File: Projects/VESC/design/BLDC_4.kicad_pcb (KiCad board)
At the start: 4 copper layers, 116 parts, among them P10 AMP17614426-2_EDGE, Q1 IRFS7530, Q2 IRFS7530, Q3 IRFS7530, Q4 IRFS7530, Q5 IRFS7530, Q6 IRFS7530, U1 STM32F40X_LQFP64, U2 TC2117, U3 DRV8302, U401 MCP2562FD, X2 CRYSTAL_GROUND_PIN

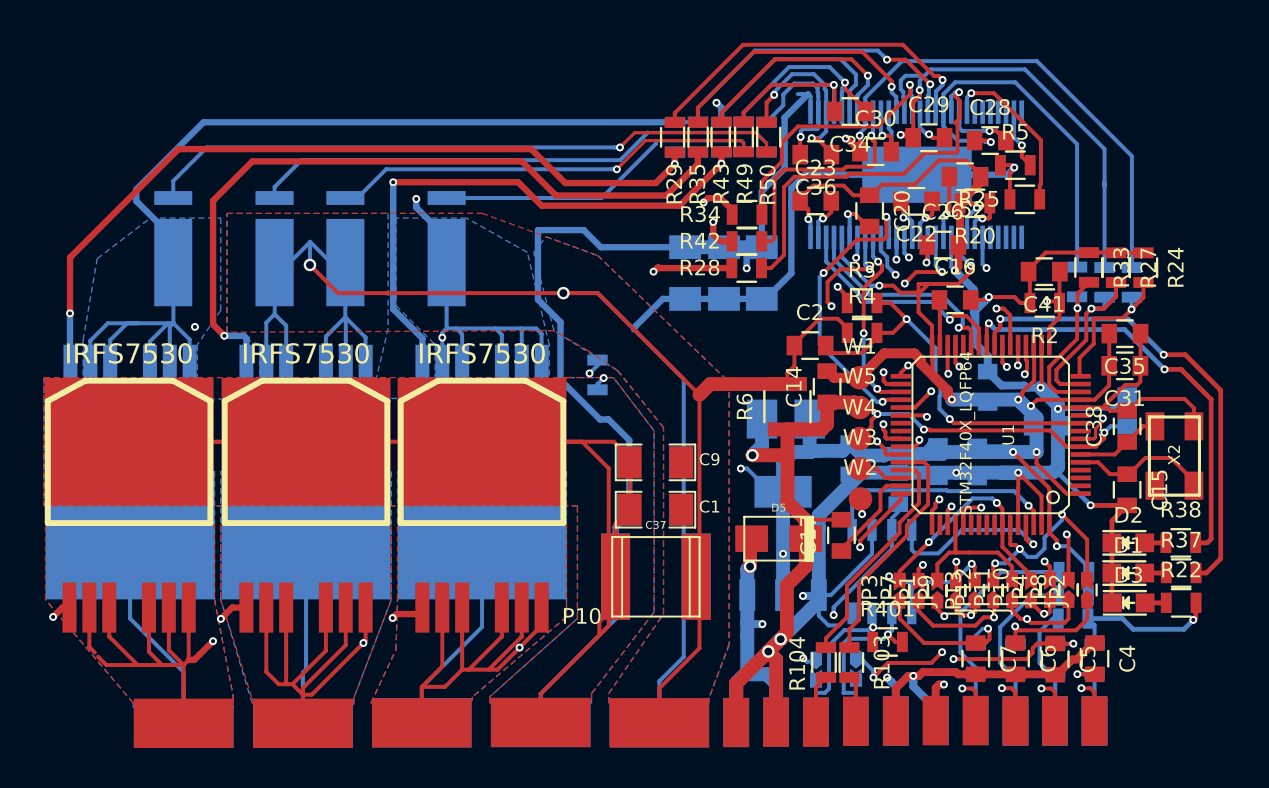
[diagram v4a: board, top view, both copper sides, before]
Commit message: more VESC card cleanup - still need to fix ground planes, via stiching, and silkscreen
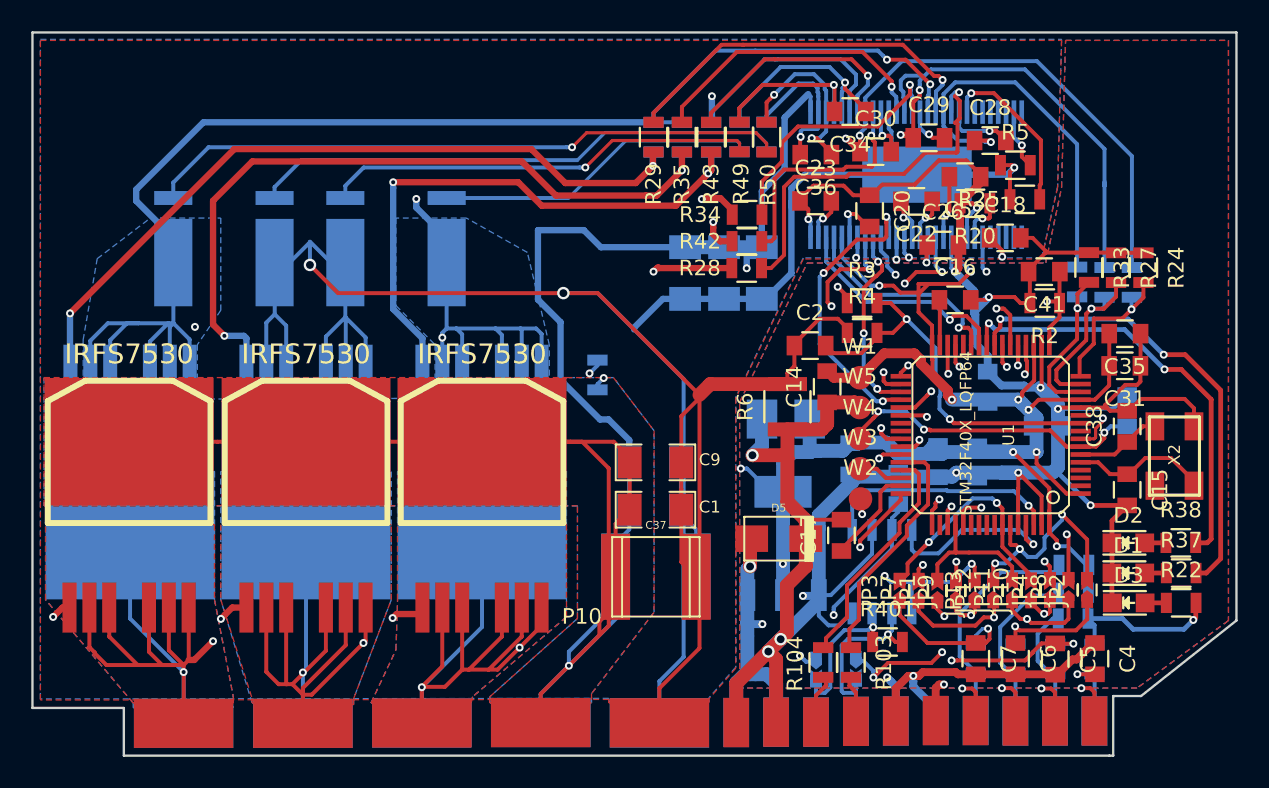
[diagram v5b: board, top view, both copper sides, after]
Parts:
- added C18: 2.2u, Capacitors_SMD:C_0805, F.Cu at (126.4, 114.0)
- moved R30 1.38 mm to (104.0, 107.5)
- moved R29 1.36 mm to (104.0, 107.5)
- moved R36 1.03 mm to (105.8, 107.5)
- moved R35 1.02 mm to (105.8, 107.5)
- moved R43 0.66 mm to (107.6, 107.5)
- moved R46 0.65 mm to (107.6, 107.5)
- moved R13 0.46 mm to (130.8, 134.9)
- moved R48 0.27 mm to (109.5, 107.5)
- moved R49 0.25 mm to (109.5, 107.5)
- moved R12 0.18 mm to (130.8, 136.7)
- moved R104 0.18 mm to (114.8, 141.1)
- moved R103 0.10 mm to (116.6, 141.1)
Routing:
- net GND: track 188.7 -> 206.0 mm
- net Net-(C18-Pad1): track 2.78 -> 9.31 mm, vias 1 -> 2
- net V_SUPPLY: track 143.2 -> 149.5 mm, vias 2 -> 3
- net VCC: track 163.4 -> 167.6 mm
- net Net-(Q2-PadG): track 51.7 -> 48.4 mm
- net GNDD: track 224.3 -> 226.9 mm
- net /Mosfet driver/H1_LOW: track 89.0 -> 90.6 mm
- net /TX_SDA: track 47.8 -> 46.4 mm
- net /Mosfet driver/M_L1: track 22.7 -> 24.1 mm
- net /Mosfet driver/M_L2: track 17.7 -> 18.7 mm
- net /W: track 143.3 -> 144.3 mm, vias 2 -> 3
- net /MCU/H1: track 21.3 -> 20.3 mm
- net /Mosfet driver/H3_LOW: track 67.8 -> 68.8 mm
- net /Mosfet driver/M_L3: track 14.4 -> 15.1 mm
- net Net-(Q4-PadG): track 47.0 -> 47.3 mm, vias 1 -> 2
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- added copper zone on B.Cu, net GNDD
- added copper zone on F.Cu, net GNDD
- added copper zone on GND, net GNDD
- added copper zone on GND2, net GNDD
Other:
- board outline added: 77 x 46.2 mm
- net class Default: clearance 0.2032 -> 0.2
- rule trace_clearance: 0.2032 -> 0.2

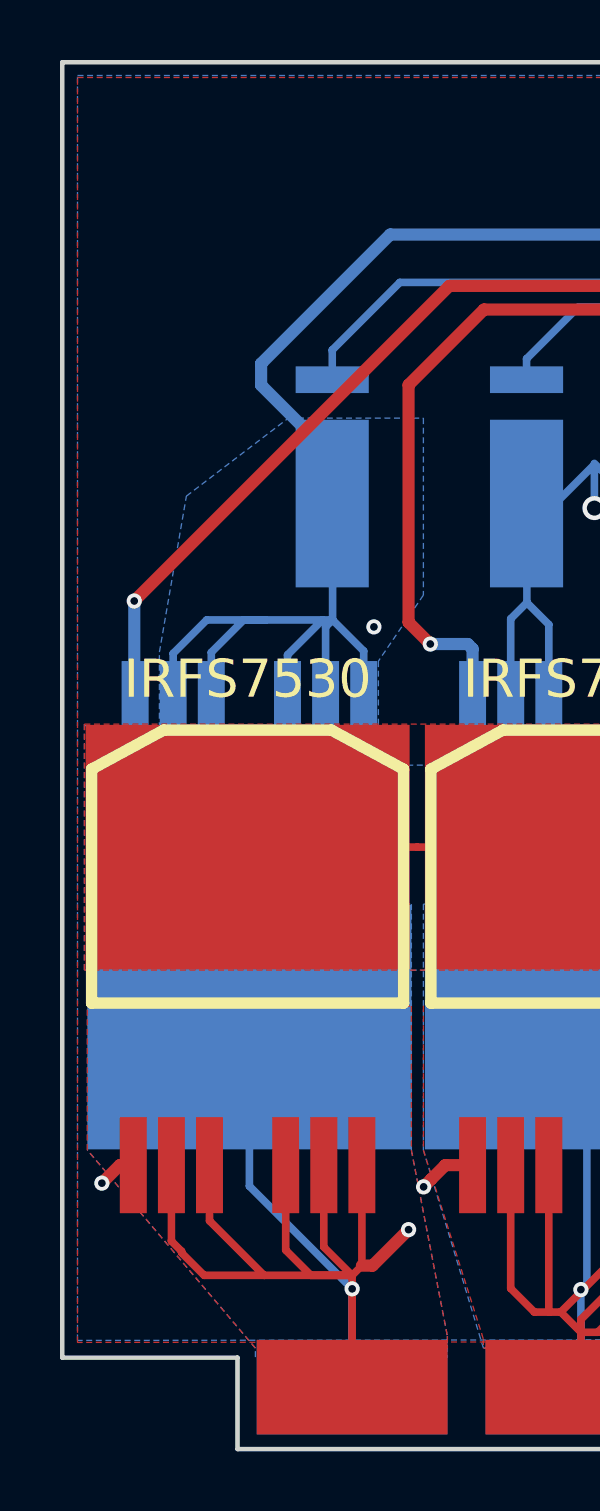
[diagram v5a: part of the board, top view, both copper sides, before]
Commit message: Added USB hub to backplane
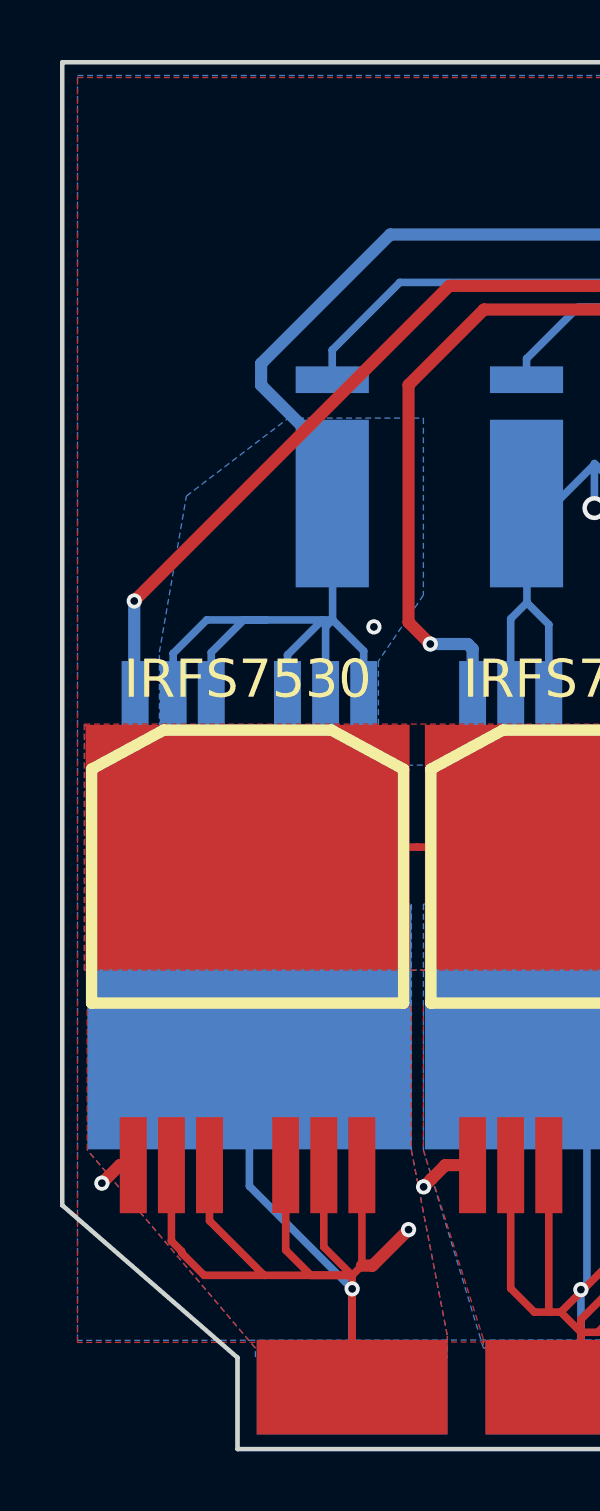
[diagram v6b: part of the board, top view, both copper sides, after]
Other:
- outline, holes or cut-outs redrawn
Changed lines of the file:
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@@
   (gr_line (start 141.224 100.838) (end 141.224 138.43) (layer Edge.Cuts) (width 0.15))
   (gr_line (start 64.262 100.838) (end 141.224 100.838) (layer Edge.Cuts) (width 0.15))
-  (gr_line (start 64.262 144.018) (end 64.262 100.838) (layer Edge.Cuts) (width 0.15))
-  (gr_line (start 70.104 144.018) (end 64.262 144.018) (layer Edge.Cuts) (width 0.15))
+  (gr_line (start 64.262 138.938) (end 64.262 100.838) (layer Edge.Cuts) (width 0.15))
+  (gr_line (start 70.104 144.018) (end 64.262 138.938) (layer Edge.Cuts) (width 0.15))
   (gr_line (start 70.104 147.066) (end 70.104 144.018) (layer Edge.Cuts) (width 0.15))
   (gr_line (start 133.096 147.066) (end 70.104 147.066) (layer Edge.Cuts) (width 0.15))

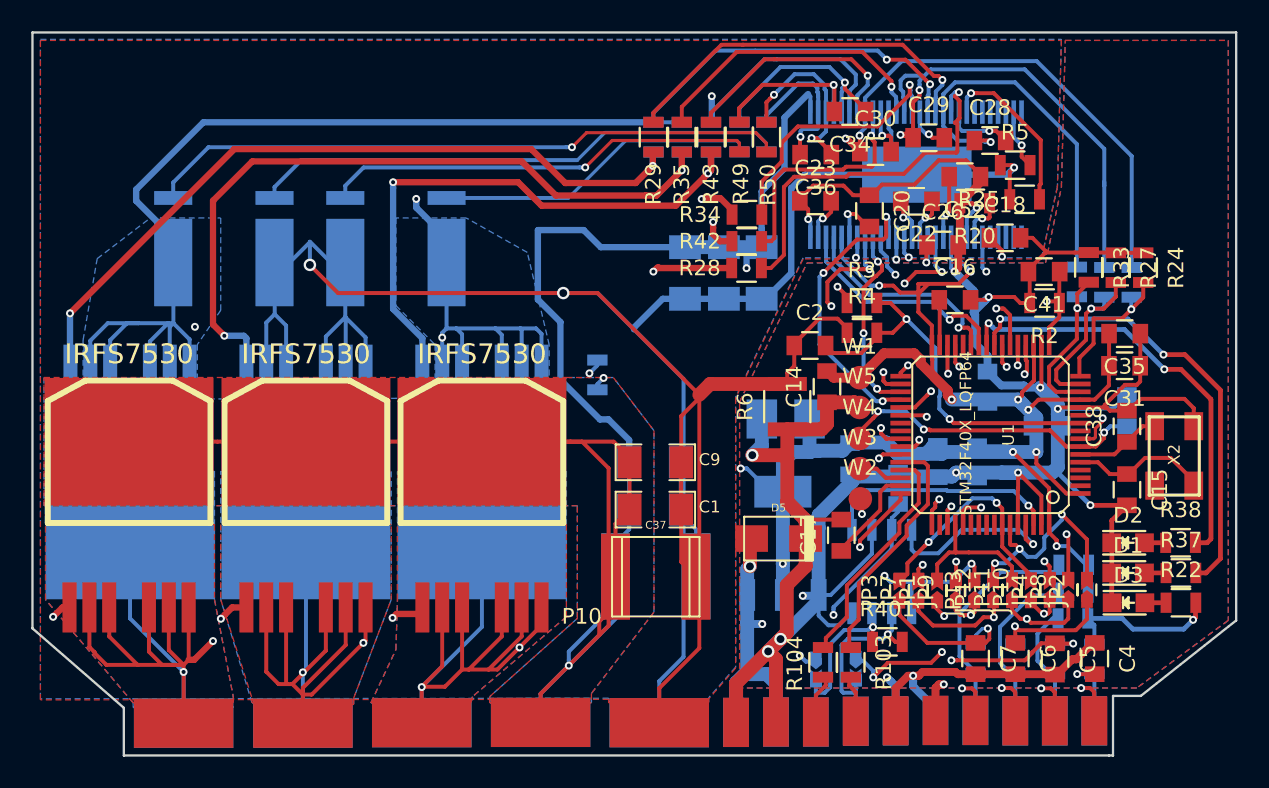
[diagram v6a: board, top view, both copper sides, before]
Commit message: Ground plane and silkscreen of VESC-R
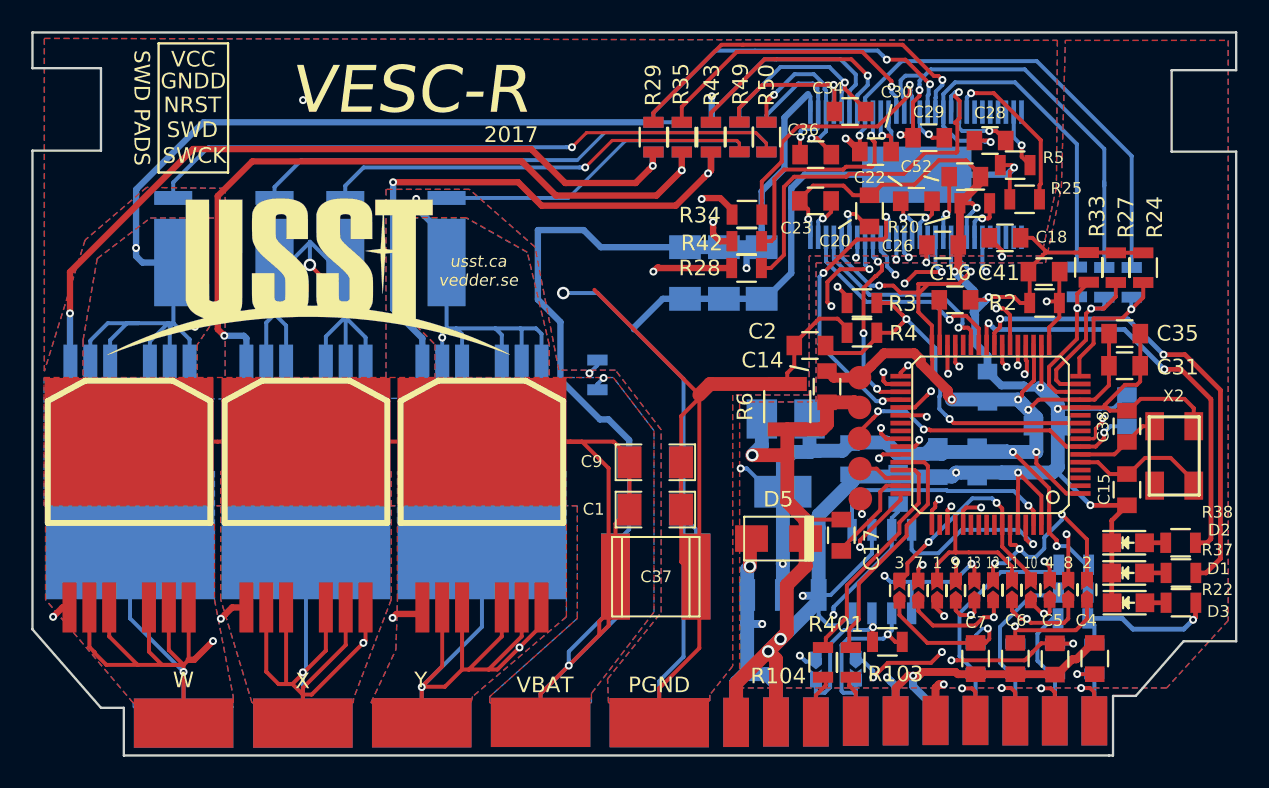
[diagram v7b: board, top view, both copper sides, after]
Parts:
- added G***: LOGO, USST-footprints:USSTLOGO, F.Cu at (81.9, 116.5)
- renumbered JP1 to 1, JP10 to 10, JP11 to 11, JP12 to 12, JP13 to 13, JP2 to 2, JP3 to 3, JP4 to 4, JP5 to 5, JP6 to 6, JP7 to 7, JP8 to 8, JP9 to 9, W5 to GNDD, W4 to NRST, W2 to SWCK, W3 to SWD, W1 to VCC
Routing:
- net (no net): track 46.7 -> 53.6 mm
- net GND: track 206.0 -> 200.2 mm, vias 3 -> 4
- net Net-(Q2-PadG): track 48.4 -> 49.9 mm
- net /Mosfet driver/H1_LOW: track 90.6 -> 91.8 mm, vias 2 -> 3
- added copper zone on F.Cu, net /Mosfet driver/H1_LOW
- added copper zone on F.Cu, net /Mosfet driver/H3_LOW
- added copper zone on GND, net /W
- added copper zone on GND2, net /W
- added copper zone on GND, net /X
- added copper zone on GND2, net /X
- added copper zone on GND, net /Y
- added copper zone on GND2, net /Y
- added copper zone on GND, net V_SUPPLY
- added copper zone on GND2, net V_SUPPLY
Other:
- outline, holes or cut-outs redrawn
- board text added: "2017"
- board text added: "PGND"
- board text added: "SWD PADS"
- board text added: "T H3 H2 H1 VHALL CANL CANH 5V 5V CS SCK MI MO VSPI USB- USB+ GND GND"
- board text added: "VBAT"
- board text added: "VESC-R"
- board text added: "W"
- board text added: "X"
- board text added: "Y"
- board text added: "usst.ca vedder.se"

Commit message: Commit to save
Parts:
- P10: footprint USST-footprints:TE2007088-1_Edge -> USST-footprints:TE2007088-1_Edge_Long
- moved P10 1.62 mm to (99.4, 146.9)
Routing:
- net /H2: track 11.2 -> 15.6 mm
- net /H3: track 7.94 -> 12.4 mm
- net /H1: track 14.7 -> 19.2 mm
- net /Temp: track 25.3 -> 29.8 mm
- net /CAN_H: track 13.0 -> 17.2 mm
- net /CAN_L: track 12.1 -> 16.1 mm
- net /USB_N: track 2.98 -> 6.85 mm
- net /USB_P: track 3.13 -> 6.81 mm
- net /CardEdge/MOSI: track 10.4 -> 13.7 mm
- net /CardEdge/MISO: track 14.5 -> 15.6 mm
- net /CardEdge/CS: track 11.0 -> 12.1 mm
- net /CardEdge/SCK: track 13.3 -> 14.4 mm
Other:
- board size 77 x 46.2 mm -> 77 x 48.7 mm
- board text added: "T H3 H2 H1 VHALL CANL CANH 5V 5V CS SCK MI MO VSPI USB- USB+ GND GND **"
- board text added: "↑"
- board text removed: "T H3 H2 H1 VHALL CANL CANH 5V 5V CS SCK MI MO VSPI USB- USB+ GND GND"
